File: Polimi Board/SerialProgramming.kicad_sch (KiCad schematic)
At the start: 13 parts, among them J1 USB_B_Micro, U2 FT2232D

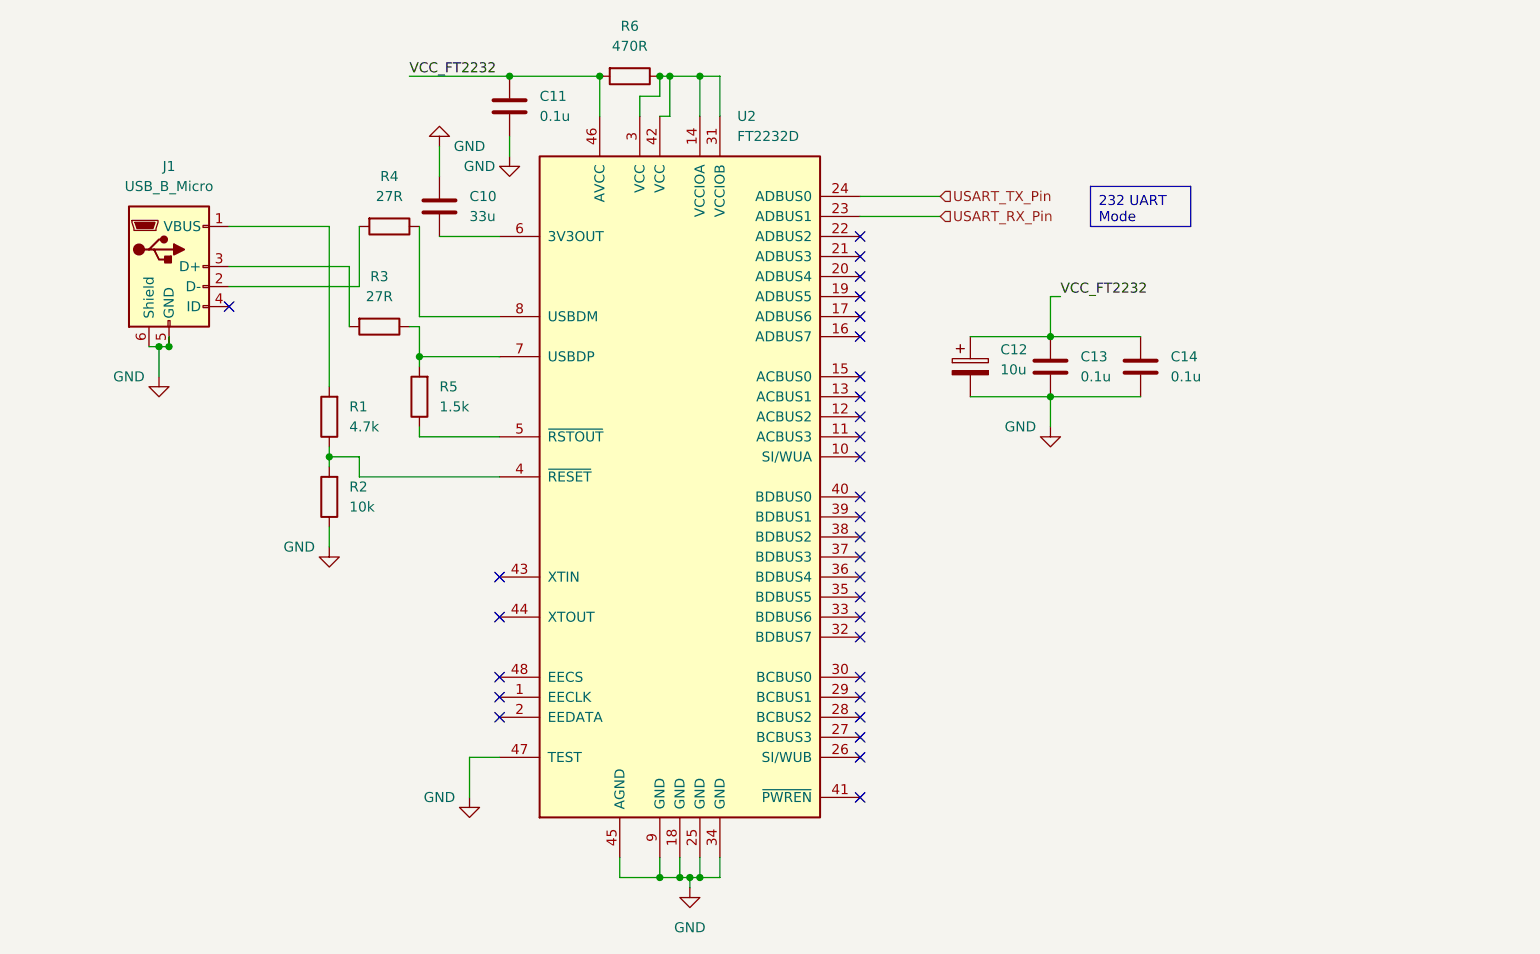
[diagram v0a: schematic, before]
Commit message: Added GPIOs
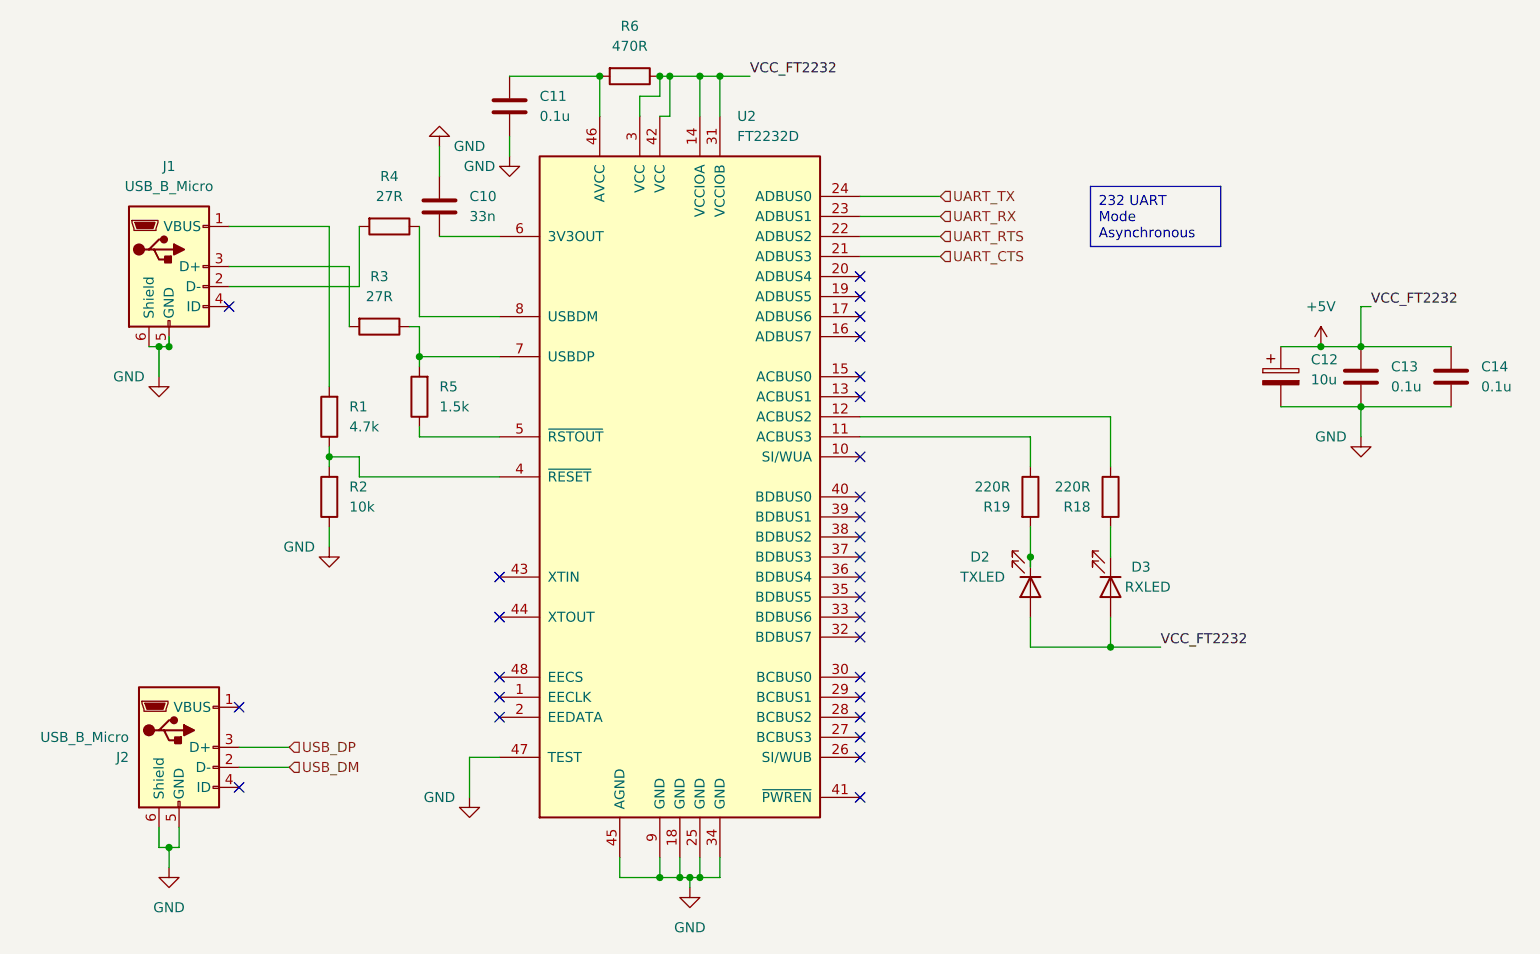
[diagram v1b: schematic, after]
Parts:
- added D2: TXLED, symbol Device:LED
- added D3: RXLED, symbol Device:LED
- added J2: USB_B_Micro, symbol Connector:USB_B_Micro
- added R18, R19: 220R, symbol Device:R
- C10: value 33u -> 33n
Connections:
- net GND: now also J2.5 (GND), J2.6 (Shield)
- net at U2.11 (ACBUS3): now also R19.1
- net at U2.12 (ACBUS2): now also R18.1
- net +5V: now reaches R6.1, U2.14 (VCCIOA), U2.3 (VCC), U2.31 (VCCIOB), U2.42 (VCC)
- net +5V: now also C12.1, C13.2, C14.2, D2.2 (A), D3.2 (A)
- net UART_CTS: now reaches U2.21 (ADBUS3)
- net UART_RTS: now reaches U2.22 (ADBUS2)
- net USART_RX_Pin renamed UART_RX
- net USART_TX_Pin renamed UART_TX
- net VCC_FT2232: no longer names the net of C11.1, R6.2, U2.46 (AVCC)
- net VCC_FT2232: no longer C12.1, C13.2, C14.2
- new net: D2.1 (K), R19.2
- new net: D3.1 (K), R18.2
- new net USB_DM: J2.2 (D-)
- new net USB_DP: J2.3 (D+)
- no-connect marks 31 -> 29
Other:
- moved on the sheet: C12, C13, C14

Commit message: Finish schematic part
To be reviewd
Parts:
- added R30: 100k, symbol Device:R
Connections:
- net GND: now also R30.1; no longer J1.6 (Shield), J2.5 (GND), J2.6 (Shield)
- new net: J2.5 (GND), R30.2
- new net Earth: J1.6 (Shield), J2.6 (Shield)
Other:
- moved on the sheet: J1, R4

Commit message: Fatte modifiche
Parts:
- added C29, C30, C31, C32: C, symbol Device:C
- added J3: Conn_ARM_JTAG_SWD_20, Connector_IDC:IDC-Header_2x10_P2.54mm_Vertical, symbol Connector:Conn_ARM_JTAG_SWD_20
- added J8: Jack-DC, Connector_BarrelJack:BarrelJack_SwitchcraftConxall_RAPC10U_Horizontal, symbol Connector:Jack-DC
- added JP3: Jumper_3_Open, symbol Jumper:Jumper_3_Open
- added U4, U7: MCP1826S, Package_TO_SOT_SMD:SOT-223-3_TabPin2, symbol Regulator_Linear:MCP1826S
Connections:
- net GND: now also C29.2, C30.2, C31.2, C32.2, J8.2, U4.2 (GND), U7.2 (GND)
- new net: C29.1, C30.1, J8.1, U4.1 (VI), U7.1 (VI)
- new net: J3.10 (GND), J3.12 (GND), J3.14 (GND), J3.16 (GND), J3.18 (GND), J3.20 (GND), J3.4 (GND), J3.6 (GND), J3.8 (GND)
- new net +3.3V: C32.1, U7.3 (VO)
- new net Vdd_out_3V3: C31.1, U4.3 (VO)
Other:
- note added: "FT2232D Power dissipation with Vcc = 5.25V 500mW"
- note added: "Jumper Choose power btw USB1 or USB2"
- moved on the sheet: C12, C13, C14

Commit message: Update the design with new specifications
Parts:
- removed C29, C30, C31, C32: C, symbol Device:C
- removed J8: Jack-DC, Connector_BarrelJack:BarrelJack_SwitchcraftConxall_RAPC10U_Horizontal, symbol Connector:Jack-DC
- removed U4, U7: MCP1826S, Package_TO_SOT_SMD:SOT-223-3_TabPin2, symbol Regulator_Linear:MCP1826S
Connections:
- net +5V: now also J3.1 (VTREF), J3.2 (VCC/NC)
- net GND: now also J3.10 (GND), J3.12 (GND), J3.14 (GND), J3.16 (GND), J3.18 (GND), J3.20 (GND), J3.4 (GND), J3.6 (GND), J3.8 (GND)
- net UART_CTS: now also U2.37 (BDBUS3); no longer U2.21 (ADBUS3)
- net UART_RTS: now also U2.38 (BDBUS2); no longer U2.22 (ADBUS2)
- net UART_RX: now also U2.39 (BDBUS1); no longer U2.23 (ADBUS1)
- net UART_TX: now also U2.40 (BDBUS0); no longer U2.24 (ADBUS0)
- net JTAG_SRST: now reaches U2.13 (ACBUS1)
- net JTAG_SRST: now also J3.15 (~{SRST})
- net JTAG_TRST: now reaches U2.15 (ACBUS0)
- net JTAG_TRST: now also J3.3 (~{TRST})
- net VBUS_PROG: now reaches J1.1 (VBUS), R1.2
- net JTAG_TD0: now reaches J3.13 (TDO/SWO)
- net JTAG_TD0: now also U2.22 (ADBUS2)
- net JTAG_TDI: now reaches J3.5 (TDI)
- net JTAG_TDI: now also U2.23 (ADBUS1)
- net JTAG_TMS: now reaches J3.7 (TMS/SWDIO)
- net JTAG_TMS: now also U2.21 (ADBUS3)
- net JTAG_TCK: now reaches J3.9 (TCK/SWCLK)
- net JTAG_TCK: now also U2.24 (ADBUS0)
- net VBUS_PROGRAMMING: now reaches JP3.1 (A)
- net USB_Vcc: now reaches JP3.2 (C)
- net VBUS_OTG: now reaches JP3.3 (B)
- net VBUS_OTG: now also J2.1 (VBUS)
- no-connect marks 29 -> 25
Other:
- note added: "Channel A and B modes can be configured with D2XX dirver"
- note added: "JTAG Connector"
- note added: "Jumper Choose 5V power btw USB1 or USB2"
- note added: "USB Self Powered Configuration of FT2232D"
- note removed: "Jumper Choose power btw USB1 or USB2"
- moved on the sheet: C10, C11, C12, C13, C14, D2, D3, J1, J2, J3, JP3, R1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

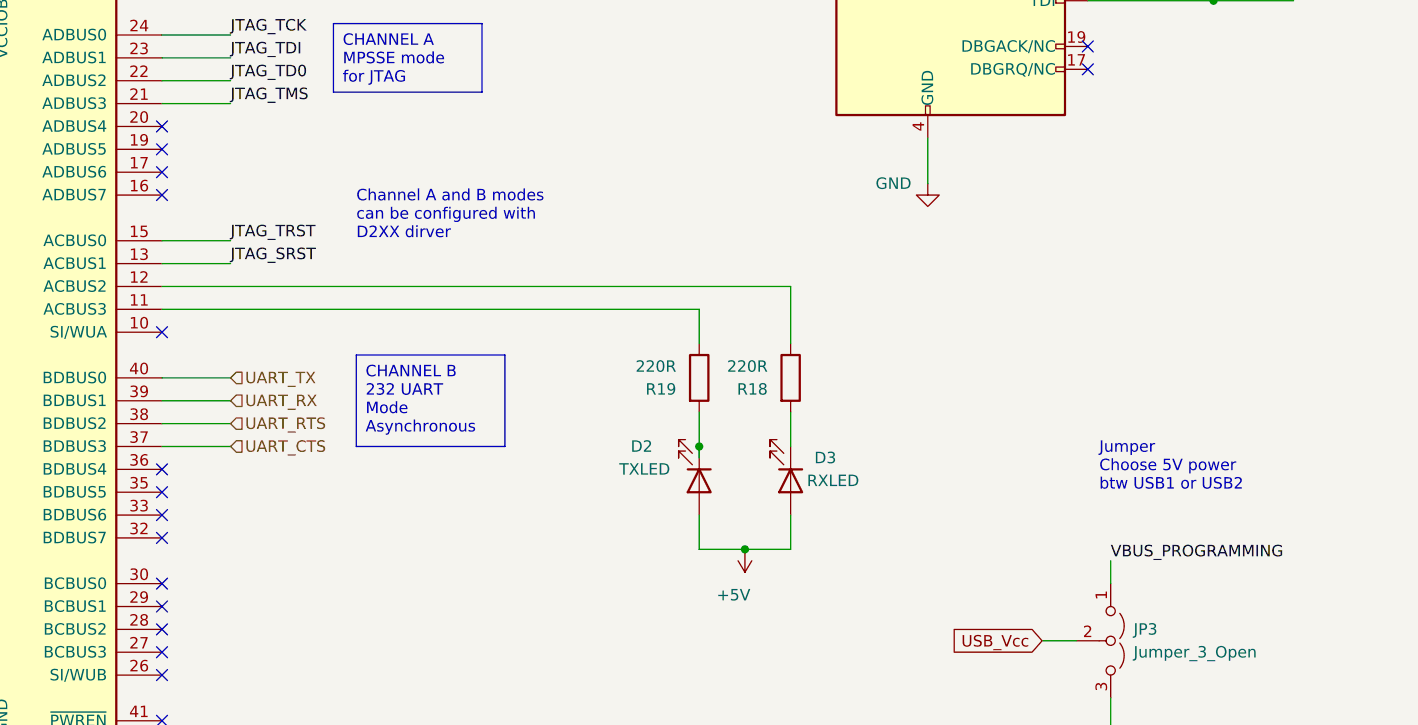
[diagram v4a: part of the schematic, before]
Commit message: Update resets and readme
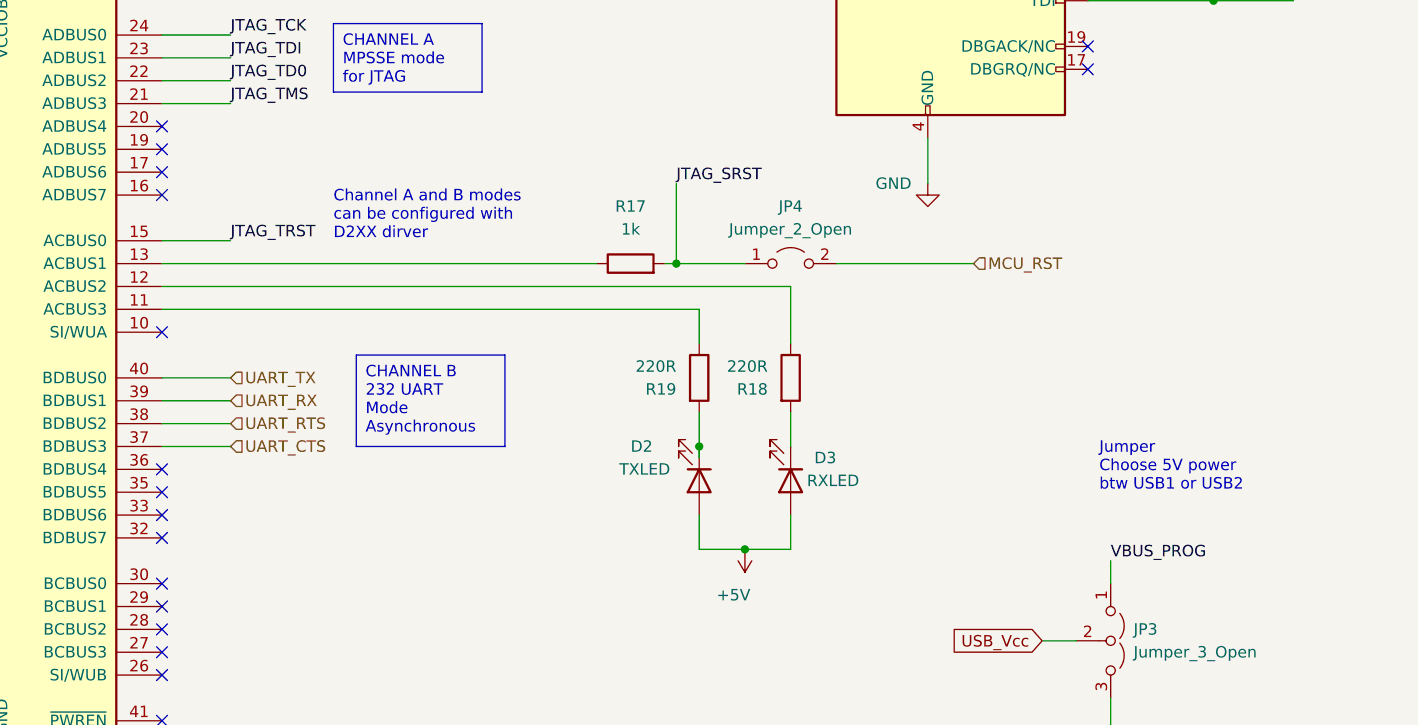
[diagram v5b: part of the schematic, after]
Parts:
- added JP4: Jumper_2_Open, TestPoint:TestPoint_2Pads_Pitch5.08mm_Drill1.3mm, symbol Jumper:Jumper_2_Open
- added R17: 1k, symbol Device:R
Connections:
- net VBUS_PROGRAMMING is gone; now on net VBUS_PROG: JP3.1 (A)
- net JTAG_SRST: now also JP4.1 (A), R17.2; no longer U2.13 (ACBUS1)
- new net: R17.1, U2.13 (ACBUS1)
- new net MCU_RST: JP4.2 (B)
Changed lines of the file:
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@@
   (title_block
     (title "Polimi Board ")
-    (date "2024-05-14")
+    (date "2024-05-15")
     (rev "2.0")
     (company "Politecnico di Milano")
@@
   )
   (junction (at 120.65 52.07) (diameter 0) (color 0 0 0 0)
+  )
+  (junction (at 195.58 92.71) (diameter 0) (color 0 0 0 0)
   )
   (junction (at 116.84 153.67) (diameter 0) (color 0 0 0 0)
@@
     (stroke (width 0) (type default))
   )
+  (wire (pts (xy 195.58 92.71) (xy 203.2 92.71))
+    (stroke (width 0) (type default))
+  )
   (wire (pts (xy 138.43 95.25) (xy 208.28 95.25))
     (stroke (width 0) (type default))
@@
     (stroke (width 0) (type default))
   )
+  (wire (pts (xy 195.58 83.82) (xy 195.58 92.71))
+    (stroke (width 0) (type default))
+  )
   (wire (pts (xy 73.66 74.93) (xy 73.66 83.82))
     (stroke (width 0) (type default))
@@
     (stroke (width 0) (type default))
   )
+  (wire (pts (xy 213.36 92.71) (xy 228.6 92.71))
+    (stroke (width 0) (type default))
+  )
   (wire (pts (xy 114.3 57.15) (xy 114.3 52.07))
     (stroke (width 0) (type default))
@@
     (stroke (width 0) (type default))
   )
+  (wire (pts (xy 138.43 92.71) (xy 186.69 92.71))
+    (stroke (width 0) (type default))
+  )
   (wire (pts (xy 255.27 63.5) (xy 264.16 63.5))
     (stroke (width 0) (type default))
@@
     (stroke (width 0) (type default))
   )
+  (wire (pts (xy 194.31 92.71) (xy 195.58 92.71))
+    (stroke (width 0) (type default))
+  )
   (wire (pts (xy 82.55 97.79) (xy 92.71 97.79))
     (stroke (width 0) (type default))
@@
   )
   (wire (pts (xy 223.52 33.02) (xy 224.79 33.02))
-    (stroke (width 0) (type default))
-  )
-  (wire (pts (xy 138.43 92.71) (xy 146.05 92.71))
     (stroke (width 0) (type default))
   )
@@
   )
   (text "Channel A and B modes\ncan be configured with\nD2XX dirver"
-    (at 160.02 90.17 0)
+    (at 157.48 90.17 0)
     (effects (font (size 1.27 1.27)) (justify left bottom))
   )
@@
     (effects (font (size 1.27 1.27)) (justify left bottom))
   )
-  (label "VBUS_PROGRAMMING" (at 243.84 125.73 0) (fields_autoplaced)
+  (label "VBUS_PROG" (at 243.84 125.73 0) (fields_autoplaced)
     (effects (font (size 1.27 1.27)) (justify left bottom))
   )
@@
     (effects (font (size 1.27 1.27)) (justify left bottom))
   )
-  (label "JTAG_SRST" (at 146.05 92.71 0) (fields_autoplaced)
+  (label "JTAG_SRST" (at 195.58 83.82 0) (fields_autoplaced)
     (effects (font (size 1.27 1.27)) (justify left bottom))
   )
@@
   )
   (hierarchical_label "USB_DM" (shape input) (at 62.23 135.89 0) (fields_autoplaced)
+    (effects (font (size 1.27 1.27)) (justify left))
+  )
+  (hierarchical_label "MCU_RST" (shape input) (at 228.6 92.71 0) (fields_autoplaced)
     (effects (font (size 1.27 1.27)) (justify left))
   )
@@
     )
   )
+  (symbol (lib_id "Device:R") (at 190.5 92.71 90) (unit 1)
+    (in_bom yes) (on_board yes) (dnp no) (fields_autoplaced)
+    (property "Reference" "R17" (at 190.5 86.36 90)
+      (effects (font (size 1.27 1.27)))
+    )
+    (property "Value" "1k" (at 190.5 88.9 90)
+      (effects (font (size 1.27 1.27)))
+    )
+    (property "Footprint" "" (at 190.5 94.488 90)
+      (effects (font (size 1.27 1.27)) hide)
+    )
+    (property "Datasheet" "~" (at 190.5 92.71 0)
+      (effects (font (size 1.27 1.27)) hide)
+    )
+    (pin "2")
+    (pin "1")
+    (instances
+      (project "Polimi Board"
+        (path "/319fe76e-1f98-44b3-99b0-af1a9ad7322c/e865888c-a3d0-46cb-8bab-3f3f2de35235"
+          (reference "R17") (unit 1)
+        )
+      )
+    )
+  )
   (symbol (lib_id "Device:C_Polarized") (at 26.67 31.75 0) (unit 1)
     (in_bom yes) (on_board yes) (dnp no) (fields_autoplaced)
@@
         )
       )
+    )
+  )
+  (symbol (lib_id "Jumper:Jumper_2_Open") (at 208.28 92.71 0) (unit 1)
+    (in_bom yes) (on_board yes) (dnp no) (fields_autoplaced)
+    (property "Reference" "JP4" (at 208.28 86.36 0)
+      (effects (font (size 1.27 1.27)))
+    )
+    (property "Value" "Jumper_2_Open" (at 208.28 88.9 0)
+      (effects (font (size 1.27 1.27)))
+    )
+    (property "Footprint" "TestPoint:TestPoint_2Pads_Pitch5.08mm_Drill1.3mm" (at 208.28 92.71 0)
+      (effects (font (size 1.27 1.27)) hide)
+    )
+    (property "Datasheet" "~" (at 208.28 92.71 0)
+      (effects (font (size 1.27 1.27)) hide)
+    )
+    (pin "2")
+    (pin "1")
+    (instances
+      (project "Polimi Board"
+        (path "/319fe76e-1f98-44b3-99b0-af1a9ad7322c/e865888c-a3d0-46cb-8bab-3f3f2de35235"
+          (reference "JP4") (unit 1)
+        )
+      )

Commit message: Added changes to the design
Ready for pcb design
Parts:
- removed C10: 33n, symbol Device:C
- removed C11: 0.1u, symbol Device:C
- removed C12: 10u, symbol Device:C_Polarized
- removed D2: TXLED, symbol Device:LED
- removed D3: RXLED, symbol Device:LED
- removed J1: USB_B_Micro, symbol Connector:USB_B_Micro
- removed JP4: Jumper_2_Open, TestPoint:TestPoint_2Pads_Pitch5.08mm_Drill1.3mm, symbol Jumper:Jumper_2_Open
- removed R17: 1k, symbol Device:R
- removed R18, R19: 220R, symbol Device:R
- removed R2: 10k, symbol Device:R
- removed R3, R4: 27R, symbol Device:R
- removed R5: 1.5k, symbol Device:R
- removed R6: 470R, symbol Device:R
- removed U2: FT2232D, Package_QFP:LQFP-48_7x7mm_P0.5mm, symbol Interface_USB:FT2232D
- added C12, C23, C24, C25, C26, C30, C33: 100nF, symbol Device:C
- added C27, C32: 4.7uF, Capacitor_SMD:C_0201_0603Metric_Pad0.64x0.40mm_HandSolder, symbol Device:C_Polarized
- added C34: 3.3uF, symbol Device:C
- added C35, C36: 27pF, symbol Device:C
- added D1: TXLED, symbol Device:LED
- added D6: RXLED, symbol Device:LED
- added J4: USB_B_Micro, symbol Connector:USB_B_Micro
- added J8: Conn_01x03_Pin, Connector_PinHeader_2.54mm:PinHeader_1x03_P2.54mm_Vertical, symbol Connector:Conn_01x03_Pin
- added JP5: Jumper_2_Open, TestPoint:TestPoint_2Pads_Pitch5.08mm_Drill1.3mm, symbol Jumper:Jumper_2_Open
- added R12, R40: 1k, symbol Device:R
- added R36: 220R, symbol Device:R
- added R37: 12k, symbol Device:R
- added U5: FT2232HL, Package_QFP:LQFP-64_10x10mm_P0.5mm, symbol Interface_USB:FT2232HL
- added Y2: 12MHz, symbol Device:Crystal
- C13, C14: value 0.1u -> 100nF
- R1: value 4.7k -> 10k
- R30: value 100k -> 220R
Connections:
- net +5V: no longer C13.2, C14.2
- net Earth: now also J4.6 (Shield)
- net GND: now also J2.5 (GND), C12.1, C23.1, C24.1, C25.1, C26.1, C27.2, C30.1, C32.2, C33.1, C34.1, C35.1, C36.1, J4.5 (GND), J8.3 (Pin_3), R37.1, U5.1 (GND), U5.10 (AGND), U5.11 (GND), U5.13 (TEST), U5.15 (GND), U5.25 (GND), U5.35 (GND), U5.47 (GND), U5.5 (GND), U5.51 (GND); no longer R30.1
- net JTAG_SRST: now also JP5.1 (A), R12.2
- net JTAG_TCK: now also U5.16 (ADBUS0)
- net JTAG_TD0: now also U5.18 (ADBUS2)
- net JTAG_TDI: now also U5.17 (ADBUS1)
- net JTAG_TMS: now also U5.19 (ADBUS3)
- net JTAG_TRST: now also U5.26 (ACBUS0)
- net MCU_RST: now also JP5.2 (B)
- net UART_CTS: now also U5.41 (BDBUS3)
- net UART_RTS: now also U5.40 (BDBUS2)
- net UART_RX: now also J8.2 (Pin_2), U5.39 (BDBUS1)
- net UART_TX: now also J8.1 (Pin_1), U5.38 (BDBUS0)
- net VBUS_PROG: now also J4.1 (VBUS); no longer R1.2
- net +3.3V: now reaches R1.1
- net +3.3V: now also C23.2, C24.2, C25.2, C26.2, C27.1, C30.2, C32.1, C33.2, D1.2 (A), D6.2 (A), R40.1, U5.20 (VCCIO), U5.31 (VCCIO), U5.4 (VPHY), U5.42 (VCCIO), U5.50 (VREGIN), U5.56 (VCCIO), U5.9 (VPLL)
- net at R30.2: now also D1.1 (K); no longer J2.5 (GND)
- new net: R12.1, U5.27 (ACBUS1)
- new net: R30.1, U5.30 (ACBUS4)
- new net: D6.1 (K), R36.2
- new net: R37.2, U5.6 (REF)
- new net: C35.2, U5.2 (OSCI), Y2.1
- new net: C36.2, U5.3 (OSCO), Y2.2
- new net: R40.2, U5.14 (~{RESET})
- new net: R36.1, U5.29 (ACBUS3)
- new net: R1.2, U5.61 (EEDATA)
- new net: J4.2 (D-), U5.7 (DM)
- new net: J4.3 (D+), U5.8 (DP)
- new net +1V8: C12.2, C13.2, C14.2, C34.2, U5.12 (VCORE), U5.37 (VCORE), U5.49 (VREGOUT), U5.64 (VCORE)
- no-connect marks 25 -> 27
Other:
- note added: "FT2232HL Power dissipation with Vcc = 3.3V Amax = 70mA, P = 231mW"
- note added: "USB Self Powered Configuration of FT2232HL"
- note removed: "FT2232D Power dissipation with Vcc = 5.25V 500mW"
- note removed: "USB Self Powered Configuration of FT2232D"
- moved on the sheet: C13, C14, J2, J3, JP3
